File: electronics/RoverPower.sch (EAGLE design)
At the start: 19 parts, among them IC1 INA139, IC3 TINY25, J1 I2C/ISP, U2 L7805

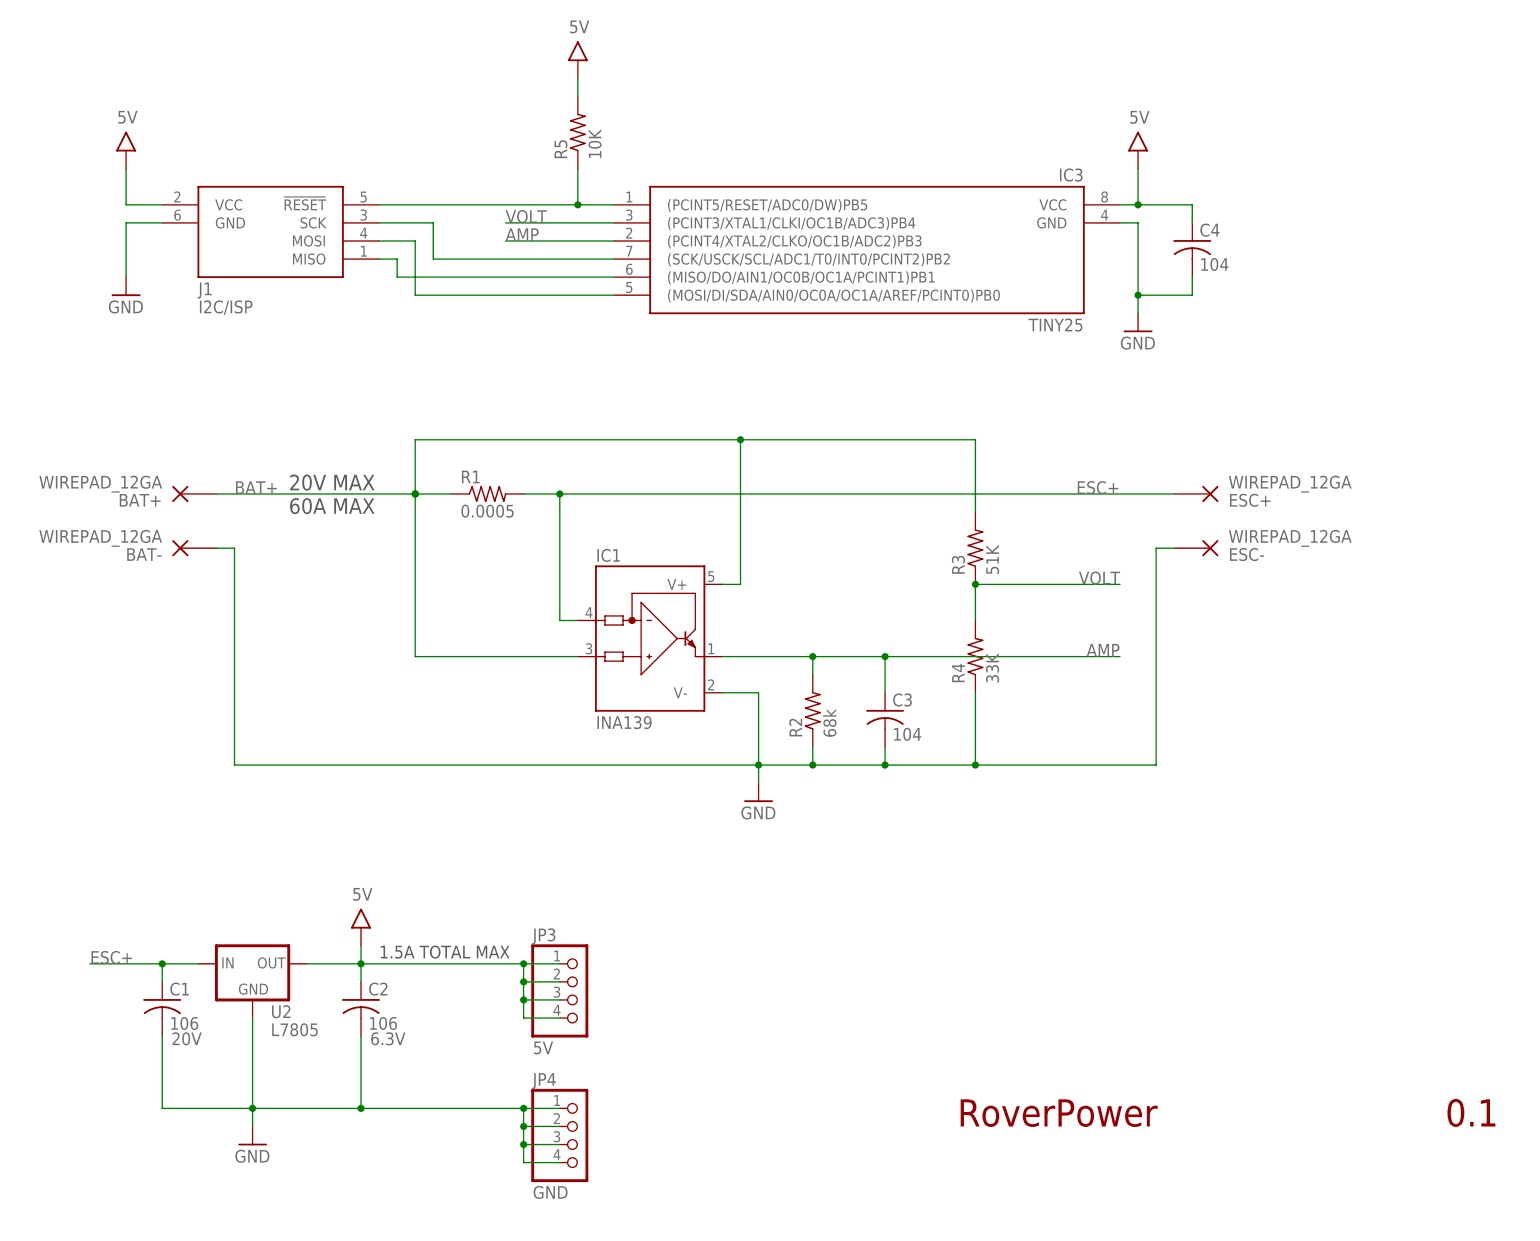
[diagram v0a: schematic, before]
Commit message: Eliminated sense, added TVS and larger capacitor for input side voltage spikes, converted to LM2940 automotive regulator, replaced 10uF output cap with Tantalum 100uF, added significant thermal dissipation features, much larger traces
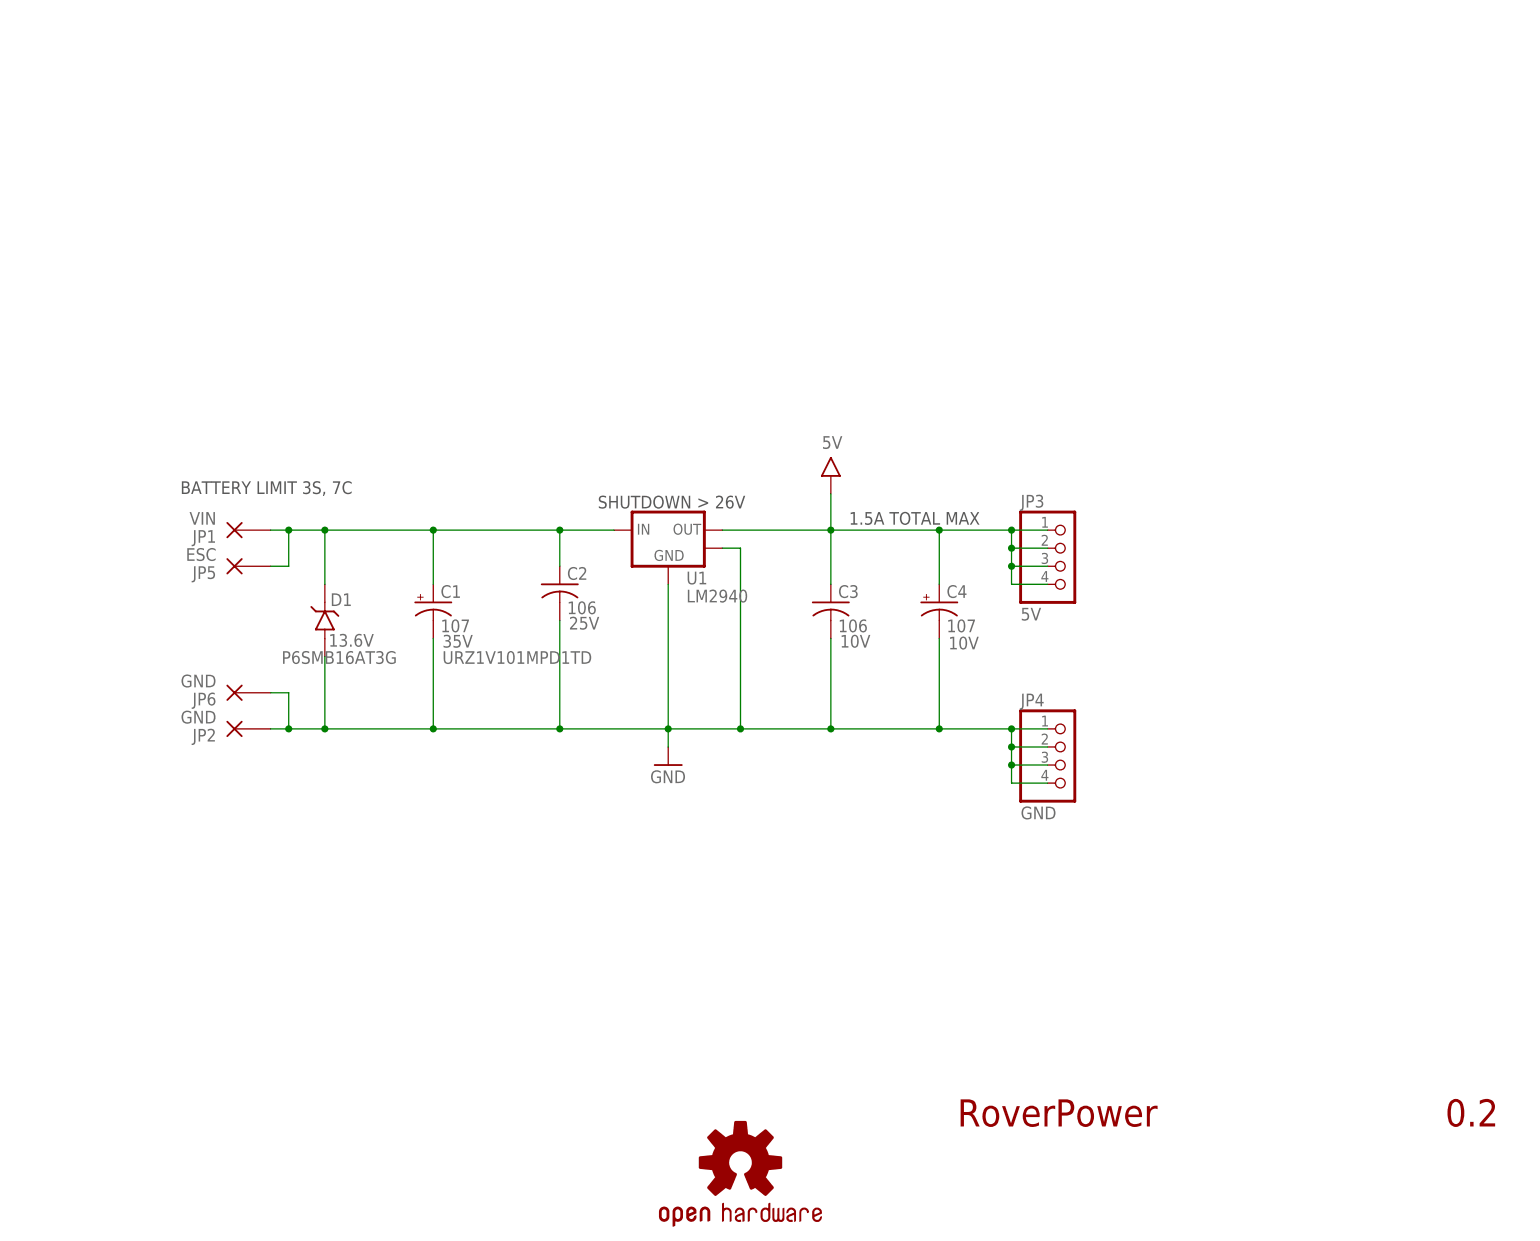
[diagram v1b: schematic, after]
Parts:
- removed BAT+, BAT-, ESC+, ESC-: WIREPAD_12GA, bt_electromech:WIREPAD_12GA
- removed IC1: INA139, burr-brown:INA168
- removed IC3: TINY25, bt_avr:TINY25/45/85-20SU
- removed J1: I2C/ISP, bt_avr:AVRISP6
- removed R1: 0.0005, bt:R-US__2512
- removed R2: 68k, rcl:R-US_R0603
- removed R3: 51K, resistor:R-US_R0603
- removed R4: 33K, resistor:R-US_R0603
- removed R5: 10K, resistor:R-US_R0603
- removed U2: L7805, v-reg-3:L78XXD2TT
- added D1: 13.6V, bt_diode:P6SMBXXAT3GSMA
- added JP1: VIN, bt_electromech:WIREPAD_12GA
- added JP2, JP6: GND, bt_electromech:WIREPAD_12GA
- added JP5: ESC, bt_electromech:WIREPAD_12GA
- added LOGO1: OSHW-LOGOS, SparkFun-Aesthetics:OSHW-LOGOS
- added U1: LM2940, bt_regulator:LM2940KTT
- C1: value 106 -> 107; device rcl:C-USC1206 -> rcl:CPOL-USE3.5-8; PARTNO (none) -> URZ1V101MPD1TD; VOLTAGE 20V -> 35V
- C2: VOLTAGE 6.3V -> 25V
- C3: value 104 -> 106; device resistor:C-USC0603 -> rcl:C-USC1206; VOLTAGE (none) -> 10V
- C4: value 104 -> 107; device rcl:C-USC0603 -> rcl:CPOL-USSMCB; VOLTAGE (none) -> 10V
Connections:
- removed net !RESET: IC3.(PCINT5/RESET/ADC0/DW)PB5, J1.!RESET, R5.1
- removed net AMP: C3.1, IC1.OUT, IC3.(PCINT4/XTAL2/CLKO/OC1B/ADC2)PB3, R2.2
- removed net ESC+: C1.1, ESC+.P, IC1.IN-, R1.2, U2.IN
- removed net MISO: IC3.(MISO/DO/AIN1/OC0B/OC1A/PCINT1)PB1, J1.MISO
- removed net SCL: IC3.(SCK/USCK/SCL/ADC1/T0/INT0/PCINT2)PB2, J1.SCK
- removed net SDA: IC3.(MOSI/DI/SDA/AIN0/OC0A/OC1A/AREF/PCINT0)PB0, J1.MOSI
- removed net VOLT: IC3.(PCINT3/XTAL1/CLKI/OC1B/ADC3)PB4, R3.1, R4.2
- net 5V: now also C3.1, C4.+, U1.VOUT; no longer C2.1, C4.1, IC3.VCC, J1.VCC, R5.2, U2.OUT
- net BAT+: now also C1.+, C2.1, D1.C, JP1.P, JP5.P, U1.VIN; no longer BAT+.P, IC1.IN+, IC1.V+, R1.1, R3.2
- net GND: now also C1.-, C4.-, D1.A, JP2.P, JP6.P, U1.GND, U1.TAB; no longer BAT-.P, C1.2, C4.2, ESC-.P, IC1.V-, IC3.GND, J1.GND, R2.1, R4.1, U2.GND
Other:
- note added: "0.2"
- note added: "BATTERY LIMIT 3S, 7C"
- note added: "SHUTDOWN > 26V"
- note removed: "0.1"
- note removed: "20V MAX"
- note removed: "60A MAX"
- moved on the sheet: C2, C3, JP3, JP4
